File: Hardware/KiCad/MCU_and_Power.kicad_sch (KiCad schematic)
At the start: 64 parts, among them SW1 SW_SPDT, SW2 SW_Push, U5 STM32H743VIT6, U6 AMS1117-5V, U7 SPX3819M5-L-3-3/TR

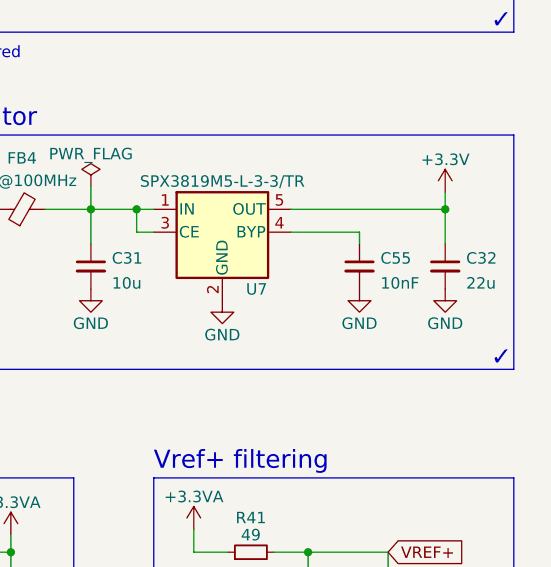
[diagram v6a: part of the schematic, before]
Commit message: Last layout optimizations and checks before production
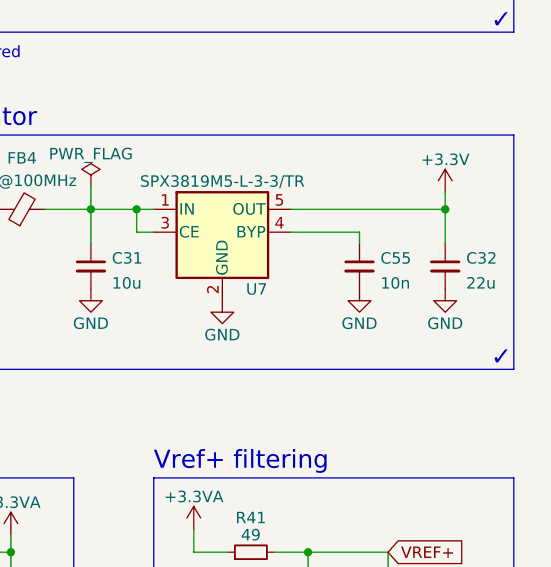
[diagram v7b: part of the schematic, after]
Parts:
- C15, C16: Comment (none) -> low ESR; JLCPCB Part# (none) -> C12530
- C17, C31: JLCPCB Part# (none) -> C96446
- C18, C19, C20, C21, C22, C23, C24, C25, C26, C27, C28, C35, C36, C39, C40, C53: JLCPCB Part# (none) -> C1525
- C29: Comment (none) -> 20V rated minimum; JLCPCB Part# (none) -> C96446
- C30, C32: JLCPCB Part# (none) -> C59461
- C33, C34: JLCPCB Part# (none) -> C32949
- C37: JLCPCB Part# (none) -> C15195
- C38: JLCPCB Part# (none) -> C15849
- C55: value 10nF -> 10n; JLCPCB Part# (none) -> C15195
- D6: JLCPCB Part# (none) -> C8598
- FB4, FB5, SW1, SW2, U5, U6, U7: JLCPCB Part# (none) -> DNP
- HSE1: JLCPCB Part# (none) -> C13738
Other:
- company: (none) -> MatvBinn
- title: (none) -> MulticopterFCS
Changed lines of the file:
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@@
 (kicad_sch (version 20211123) (generator eeschema)
   (paper "A4")
+  (title_block
+    (title "MulticopterFCS")
+    (date "2022-07-04")
+    (rev "V1.0")
+    (company "MatvBinn")
+  )
   (junction (at 212.725 62.23) (diameter 0) (color 0 0 0 0)
   )
@@
       (effects (font (size 1.27 1.27)) hide)
     )
+    (property "JLCPCB Part#" "C1525" (id 4) (at 264.16 31.75 0)
+      (effects (font (size 1.27 1.27)) hide)
+    )
     (pin "1")
     (pin "2")
@@
       (effects (font (size 1.27 1.27)) hide)
     )
+    (property "JLCPCB Part#" "C1525" (id 4) (at 248.92 144.78 0)
+      (effects (font (size 1.27 1.27)) hide)
+    )
     (pin "1")
     (pin "2")
@@
       (effects (font (size 1.27 1.27)) hide)
     )
+    (property "JLCPCB Part#" "C96446" (id 4) (at 147.32 31.75 0)
+      (effects (font (size 1.27 1.27)) hide)
+    )
     (pin "1")
     (pin "2")
@@
       (effects (font (size 1.27 1.27)) hide)
     )
+    (property "JLCPCB Part#" "C1525" (id 4) (at 226.06 31.75 0)
+      (effects (font (size 1.27 1.27)) hide)
+    )
     (pin "1")
     (pin "2")
@@
       (effects (font (size 1.27 1.27)) hide)
     )
+    (property "JLCPCB Part#" "C1525" (id 4) (at 206.375 31.75 0)
+      (effects (font (size 1.27 1.27)) hide)
+    )
     (pin "1")
     (pin "2")
@@
       (effects (font (size 1.27 1.27)) hide)
     )
+    (property "JLCPCB Part#" "DNP" (id 4) (at 217.17 141.605 0)
+      (effects (font (size 1.27 1.27)) hide)
+    )
     (pin "1")
     (pin "2")
@@
       (effects (font (size 1.27 1.27)) hide)
     )
+    (property "JLCPCB Part#" "C1525" (id 4) (at 254.635 31.75 0)
+      (effects (font (size 1.27 1.27)) hide)
+    )
     (pin "1")
     (pin "2")
@@
       (effects (font (size 1.27 1.27)) hide)
     )
+    (property "JLCPCB Part#" "C1525" (id 4) (at 196.85 31.75 0)
+      (effects (font (size 1.27 1.27)) hide)
+    )
     (pin "1")
     (pin "2")
@@
       (effects (font (size 1.27 1.27)) hide)
     )
+    (property "JLCPCB Part#" "DNP" (id 4) (at 71.12 107.315 0)
+      (effects (font (size 1.27 1.27)) hide)
+    )
     (pin "1")
     (pin "10")
@@
       (effects (font (size 1.27 1.27)) hide)
     )
+    (property "JLCPCB Part#" "C59461" (id 4) (at 172.085 69.215 0)
+      (effects (font (size 1.27 1.27)) hide)
+    )
     (pin "1")
     (pin "2")
@@
       (effects (font (size 1.27 1.27)) (justify left))
     )
-    (property "Value" "10nF" (id 1) (at 259.4991 70.4529 0)
+    (property "Value" "10n" (id 1) (at 259.4991 70.4529 0)
       (effects (font (size 1.27 1.27)) (justify left))
     )
@@
       (effects (font (size 1.27 1.27)) hide)
     )
+    (property "JLCPCB Part#" "C15195" (id 4) (at 257.175 68.58 0)
+      (effects (font (size 1.27 1.27)) hide)
+    )
     (pin "1")
     (pin "2")
@@
       (effects (font (size 1.27 1.27)) hide)
     )
+    (property "JLCPCB Part#" "C1525" (id 4) (at 260.35 106.68 0)
+      (effects (font (size 1.27 1.27)) hide)
+    )
     (pin "1")
     (pin "2")
@@
       (effects (font (size 1.27 1.27)) hide)
     )
+    (property "JLCPCB Part#" "C32949" (id 4) (at 160.02 106.68 0)
+      (effects (font (size 1.27 1.27)) hide)
+    )
     (pin "1")
     (pin "2")
@@
       (effects (font (size 1.27 1.27)) hide)
     )
+    (property "JLCPCB Part#" "C8598" (id 4) (at 204.47 62.23 0)
+      (effects (font (size 1.27 1.27)) hide)
+    )
     (pin "1")
     (pin "2")
@@
       (effects (font (size 1.27 1.27)) hide)
     )
+    (property "Comment" "low ESR" (id 4) (at 20.955 63.5 0)
+      (effects (font (size 1.27 1.27)) hide)
+    )
+    (property "JLCPCB Part#" "C12530" (id 5) (at 20.955 63.5 0)
+      (effects (font (size 1.27 1.27)) hide)
+    )
     (pin "1")
     (pin "2")
@@
       (effects (font (size 1.27 1.27)) hide)
     )
+    (property "JLCPCB Part#" "C1525" (id 4) (at 235.585 31.75 0)
+      (effects (font (size 1.27 1.27)) hide)
+    )
     (pin "1")
     (pin "2")
@@
       (effects (font (size 1.27 1.27)) hide)
     )
+    (property "JLCPCB Part#" "DNP" (id 4) (at 219.71 62.23 0)
+      (effects (font (size 1.27 1.27)) hide)
+    )
     (pin "1")
     (pin "2")
@@
       (effects (font (size 1.27 1.27)) hide)
     )
+    (property "JLCPCB Part#" "C1525" (id 4) (at 187.325 31.75 0)
+      (effects (font (size 1.27 1.27)) hide)
+    )
     (pin "1")
     (pin "2")
@@
       (effects (font (size 1.27 1.27)) hide)
     )
+    (property "JLCPCB Part#" "C1525" (id 4) (at 215.9 31.75 0)
+      (effects (font (size 1.27 1.27)) hide)
+    )
     (pin "1")
     (pin "2")
@@
       (effects (font (size 1.27 1.27)) hide)
     )
+    (property "JLCPCB Part#" "C15849" (id 4) (at 251.46 106.68 0)
+      (effects (font (size 1.27 1.27)) hide)
+    )
     (pin "1")
     (pin "2")
@@
       (effects (font (size 1.27 1.27)) hide)
     )
+    (property "JLCPCB Part#" "C1525" (id 4) (at 245.11 31.75 0)
+      (effects (font (size 1.27 1.27)) hide)
+    )
     (pin "1")
     (pin "2")
@@
       (effects (font (size 1.27 1.27)) hide)
     )
+    (property "JLCPCB Part#" "C59461" (id 4) (at 266.7 68.58 0)
+      (effects (font (size 1.27 1.27)) hide)
+    )
     (pin "1")
     (pin "2")
@@
       (effects (font (size 1.27 1.27)) hide)
     )
+    (property "JLCPCB Part#" "DNP" (id 4) (at 241.935 64.77 0)
+      (effects (font (size 1.27 1.27)) hide)
+    )
     (pin "1")
     (pin "2")
@@
       (effects (font (size 1.27 1.27)) hide)
     )
+    (property "JLCPCB Part#" "C15195" (id 4) (at 218.44 106.68 0)
+      (effects (font (size 1.27 1.27)) hide)
+    )
     (pin "1")
     (pin "2")
@@
       (effects (font (size 1.27 1.27)) hide)
     )
+    (property "JLCPCB Part#" "C1525" (id 4) (at 157.48 31.75 0)
+      (effects (font (size 1.27 1.27)) hide)
+    )
     (pin "1")
     (pin "2")
@@
       (effects (font (size 1.27 1.27)) hide)
     )
+    (property "JLCPCB Part#" "C1525" (id 4) (at 177.165 31.75 0)
+      (effects (font (size 1.27 1.27)) hide)
+    )
     (pin "1")
     (pin "2")
@@
       (effects (font (size 1.27 1.27)) hide)
     )
+    (property "JLCPCB Part#" "C32949" (id 4) (at 144.145 106.68 0)
+      (effects (font (size 1.27 1.27)) hide)
+    )
     (pin "1")
     (pin "2")
@@
       (effects (font (size 1.27 1.27)) hide)
     )
+    (property "JLCPCB Part#" "C1525" (id 4) (at 167.005 31.75 0)
+      (effects (font (size 1.27 1.27)) hide)
+    )
     (pin "1")
     (pin "2")
@@
       (effects (font (size 1.27 1.27)) hide)
     )
+    (property "Comment" "low ESR" (id 4) (at 31.75 63.5 0)
+      (effects (font (size 1.27 1.27)) hide)
+    )
+    (property "JLCPCB Part#" "C12530" (id 5) (at 31.75 63.5 0)
+      (effects (font (size 1.27 1.27)) hide)
+    )
     (pin "1")
     (pin "2")
@@
       (effects (font (size 1.27 1.27)) hide)
     )
+    (property "JLCPCB Part#" "DNP" (id 4) (at 198.12 100.33 0)
+      (effects (font (size 1.27 1.27)) hide)
+    )
     (pin "1")
     (pin "2")
@@
       (effects (font (size 1.27 1.27)) hide)
     )
+    (property "JLCPCB Part#" "C13738" (id 4) (at 149.86 100.33 0)
+      (effects (font (size 1.27 1.27)) hide)
+    )
     (pin "1")
     (pin "2")
@@
       (effects (font (size 1.27 1.27)) hide)
     )
+    (property "Comment" "20V rated minimum" (id 4) (at 143.51 69.215 0)
+      (effects (font (size 1.27 1.27)) hide)
+    )
+    (property "JLCPCB Part#" "C96446" (id 5) (at 143.51 69.215 0)
+      (effects (font (size 1.27 1.27)) hide)
+    )
     (pin "1")
     (pin "2")
@@
       (effects (font (size 1.27 1.27)) hide)
     )
+    (property "JLCPCB Part#" "C96446" (id 4) (at 227.33 68.58 0)
+      (effects (font (size 1.27 1.27)) hide)
+    )
     (pin "1")
     (pin "2")
@@
       (effects (font (size 1.27 1.27)) hide)
     )
+    (property "JLCPCB Part#" "DNP" (id 4) (at 262.255 140.335 0)
+      (effects (font (size 1.27 1.27)) hide)
+    )
     (pin "1")
     (pin "2")
@@
       (effects (font (size 1.27 1.27)) hide)
     )
+    (property "JLCPCB Part#" "C1525" (id 4) (at 205.74 106.68 0)
+      (effects (font (size 1.27 1.27)) hide)
+    )
     (pin "1")
     (pin "2")
@@
       (effects (font (size 1.27 1.27)) hide)
     )
+    (property "JLCPCB Part#" "C1525" (id 4) (at 189.865 106.68 0)
+      (effects (font (size 1.27 1.27)) hide)
+    )
     (pin "1")
     (pin "2")
@@
       (effects (font (size 1.27 1.27)) hide)
     )
+    (property "JLCPCB Part#" "DNP" (id 4) (at 160.02 62.865 0)
+      (effects (font (size 1.27 1.27)) hide)
+    )

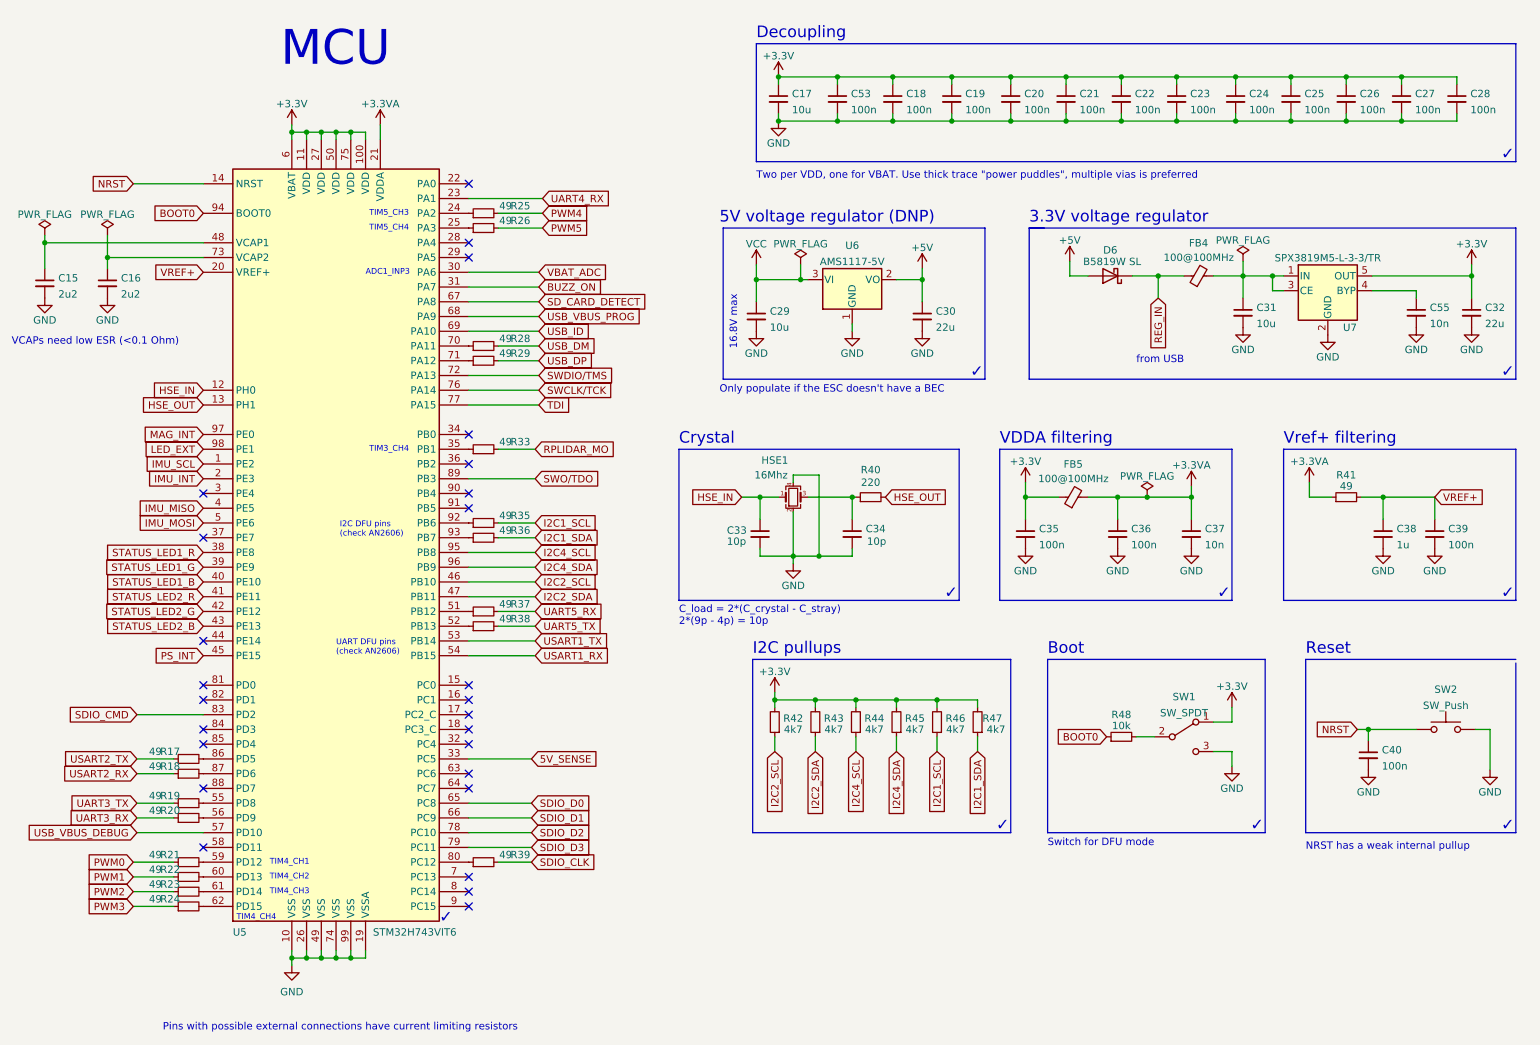
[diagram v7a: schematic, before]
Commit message: Finalizing V1.0 PCB, design send off for production
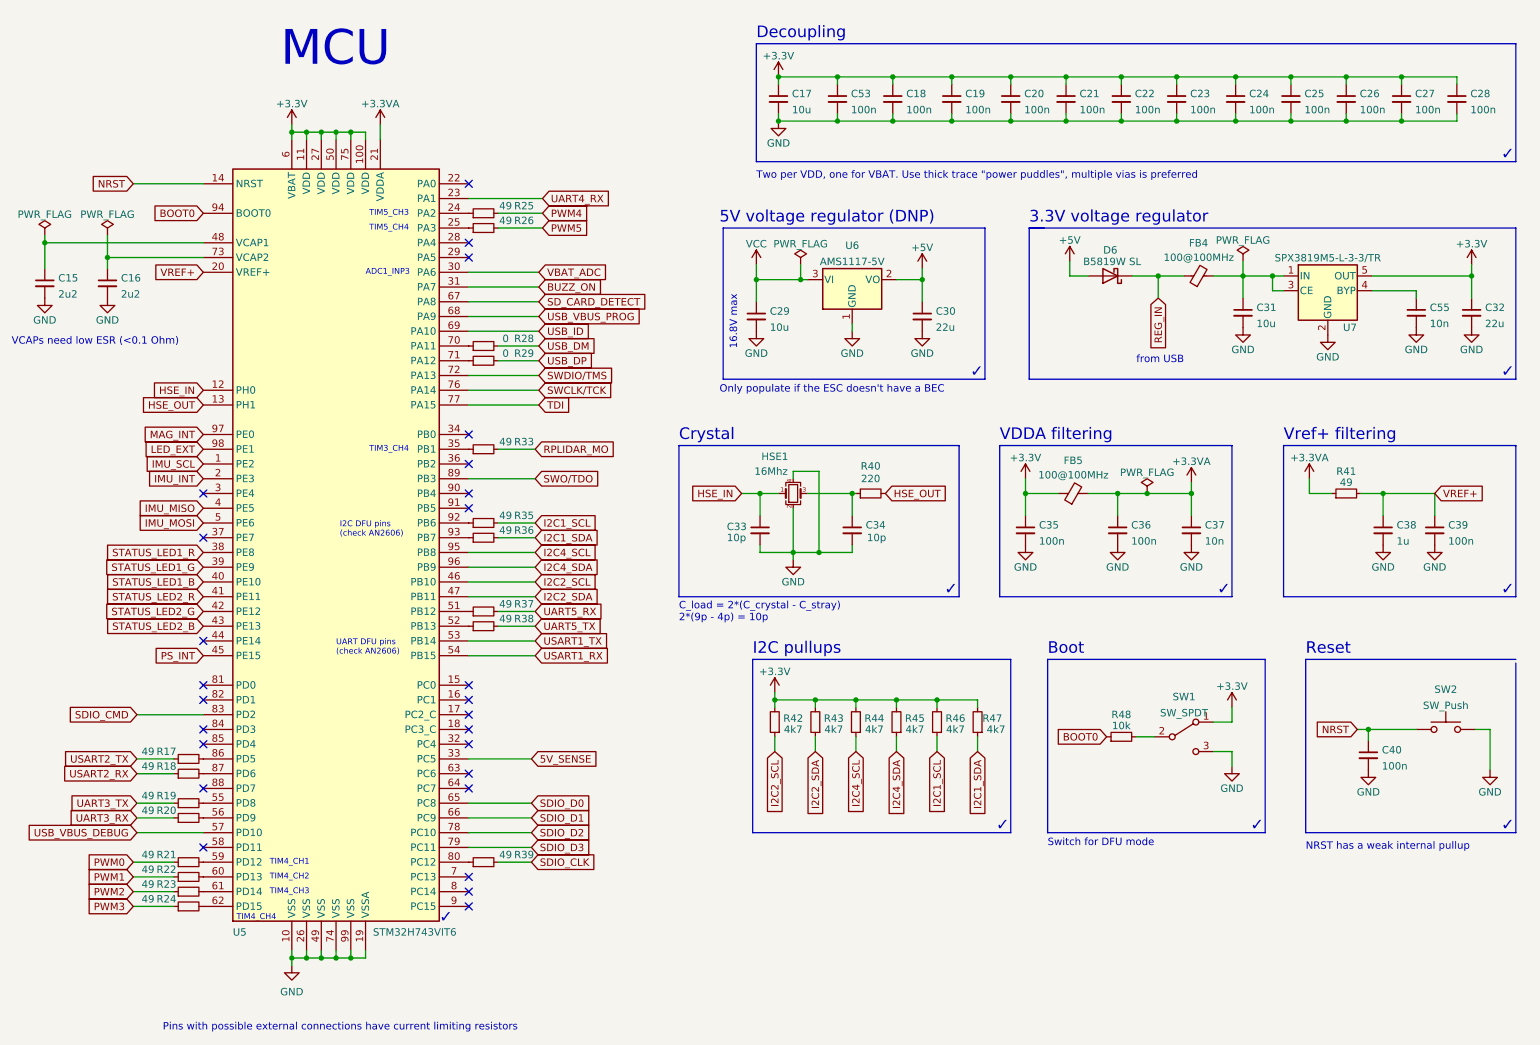
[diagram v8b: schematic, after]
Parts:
- R28, R29: value 49 -> 0
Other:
- moved on the sheet: C33, C34, C35, C36, C37, C38, C39, FB5, HSE1, R40, R41
